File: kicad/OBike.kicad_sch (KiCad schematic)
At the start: 58 parts, among them J1 Conn_01x04, J3 Conn_01x02, J4 Conn_01x03, J5 Conn_01x08, J6 Conn_01x02, J7 Conn_01x04, J8 Micro_SD_Card_Det1, SW1 5_position_tactile, U1 DPS368XTSA1, U2 DS3231M, U3 MCP23017_SO, U4 74HC14, U5 Seeed Studio XIAO SAMD21

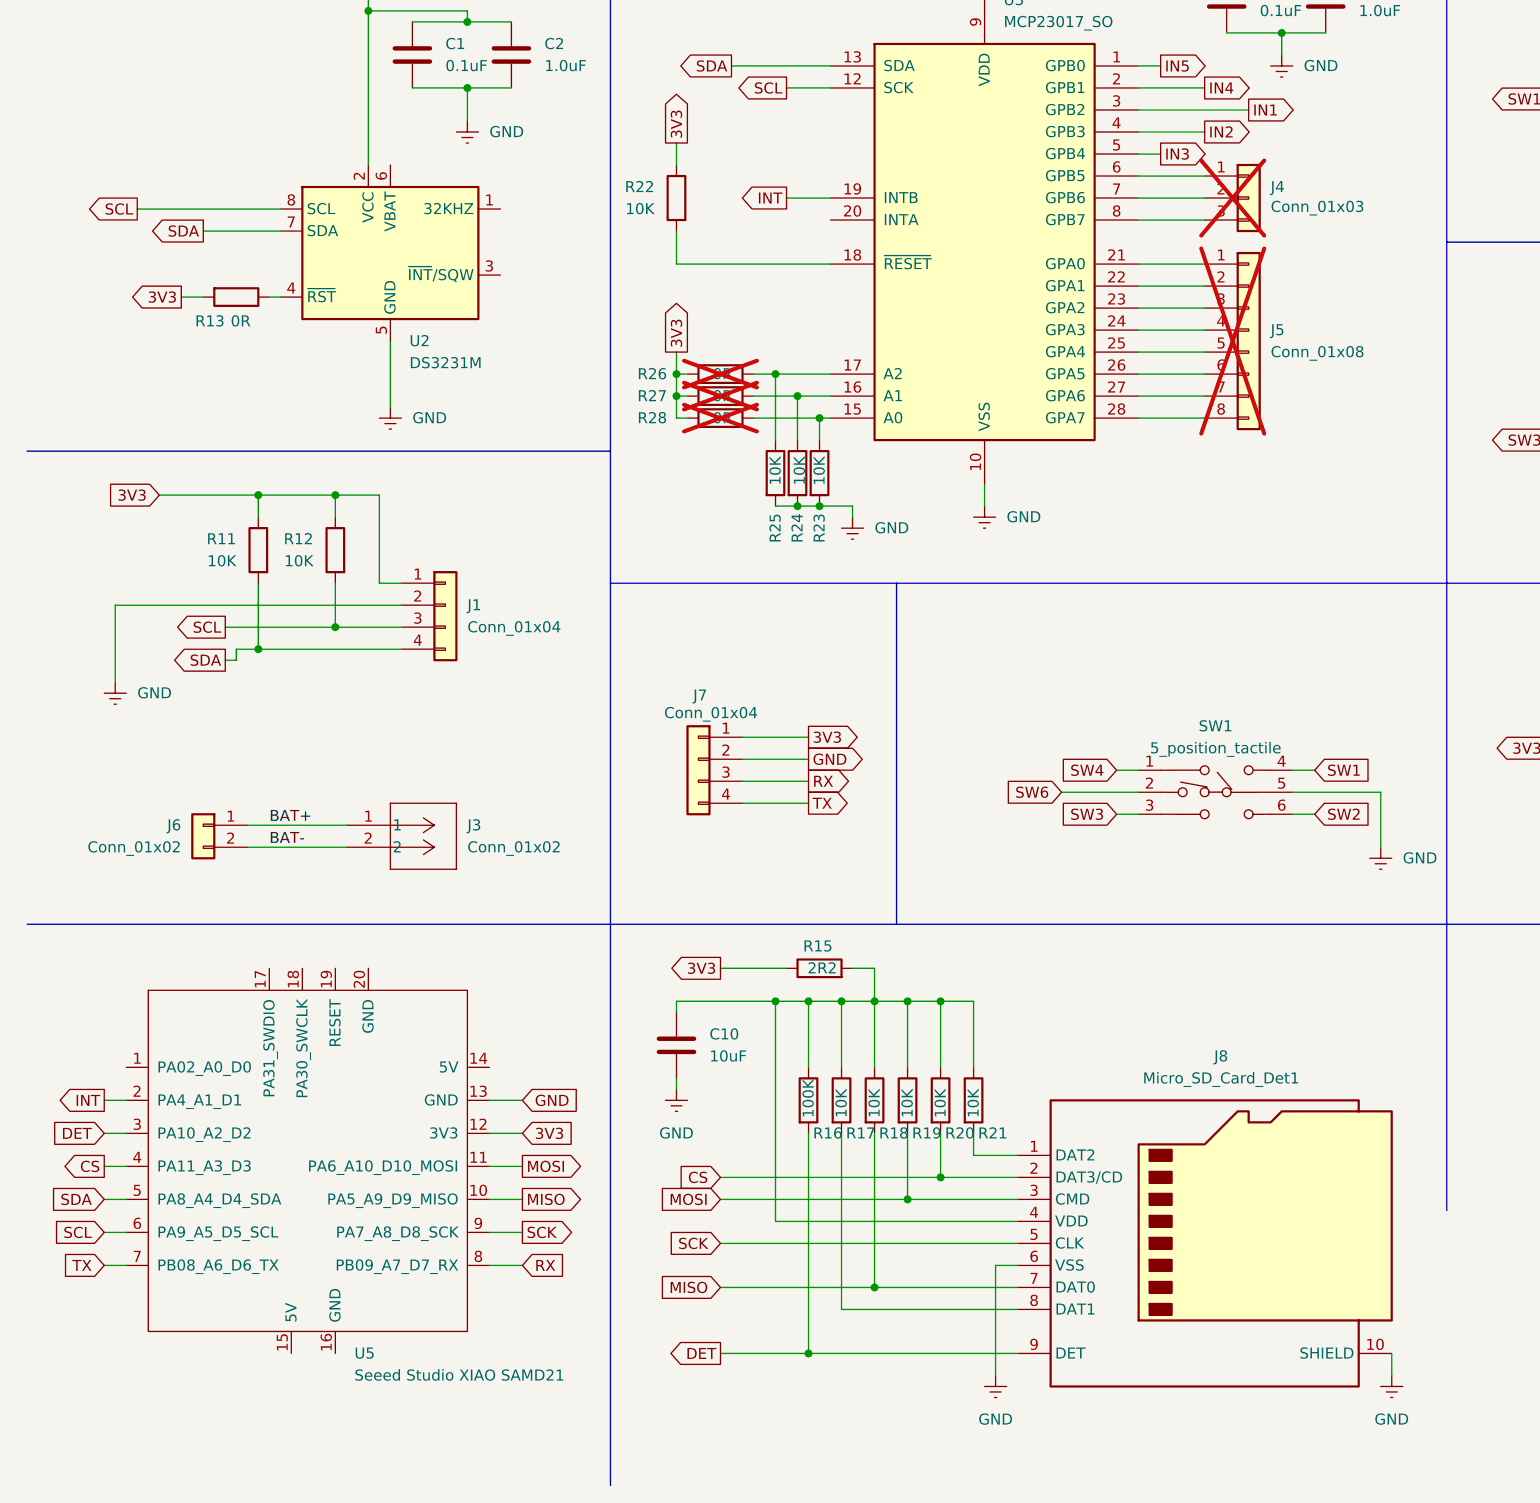
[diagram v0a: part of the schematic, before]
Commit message: 1.69" TFT
Changed screen connections to suit an SPI screen
Changed the arduino project to use the adafruit ST7789 library
Intended LCD is the wavshare 1.69" LCD
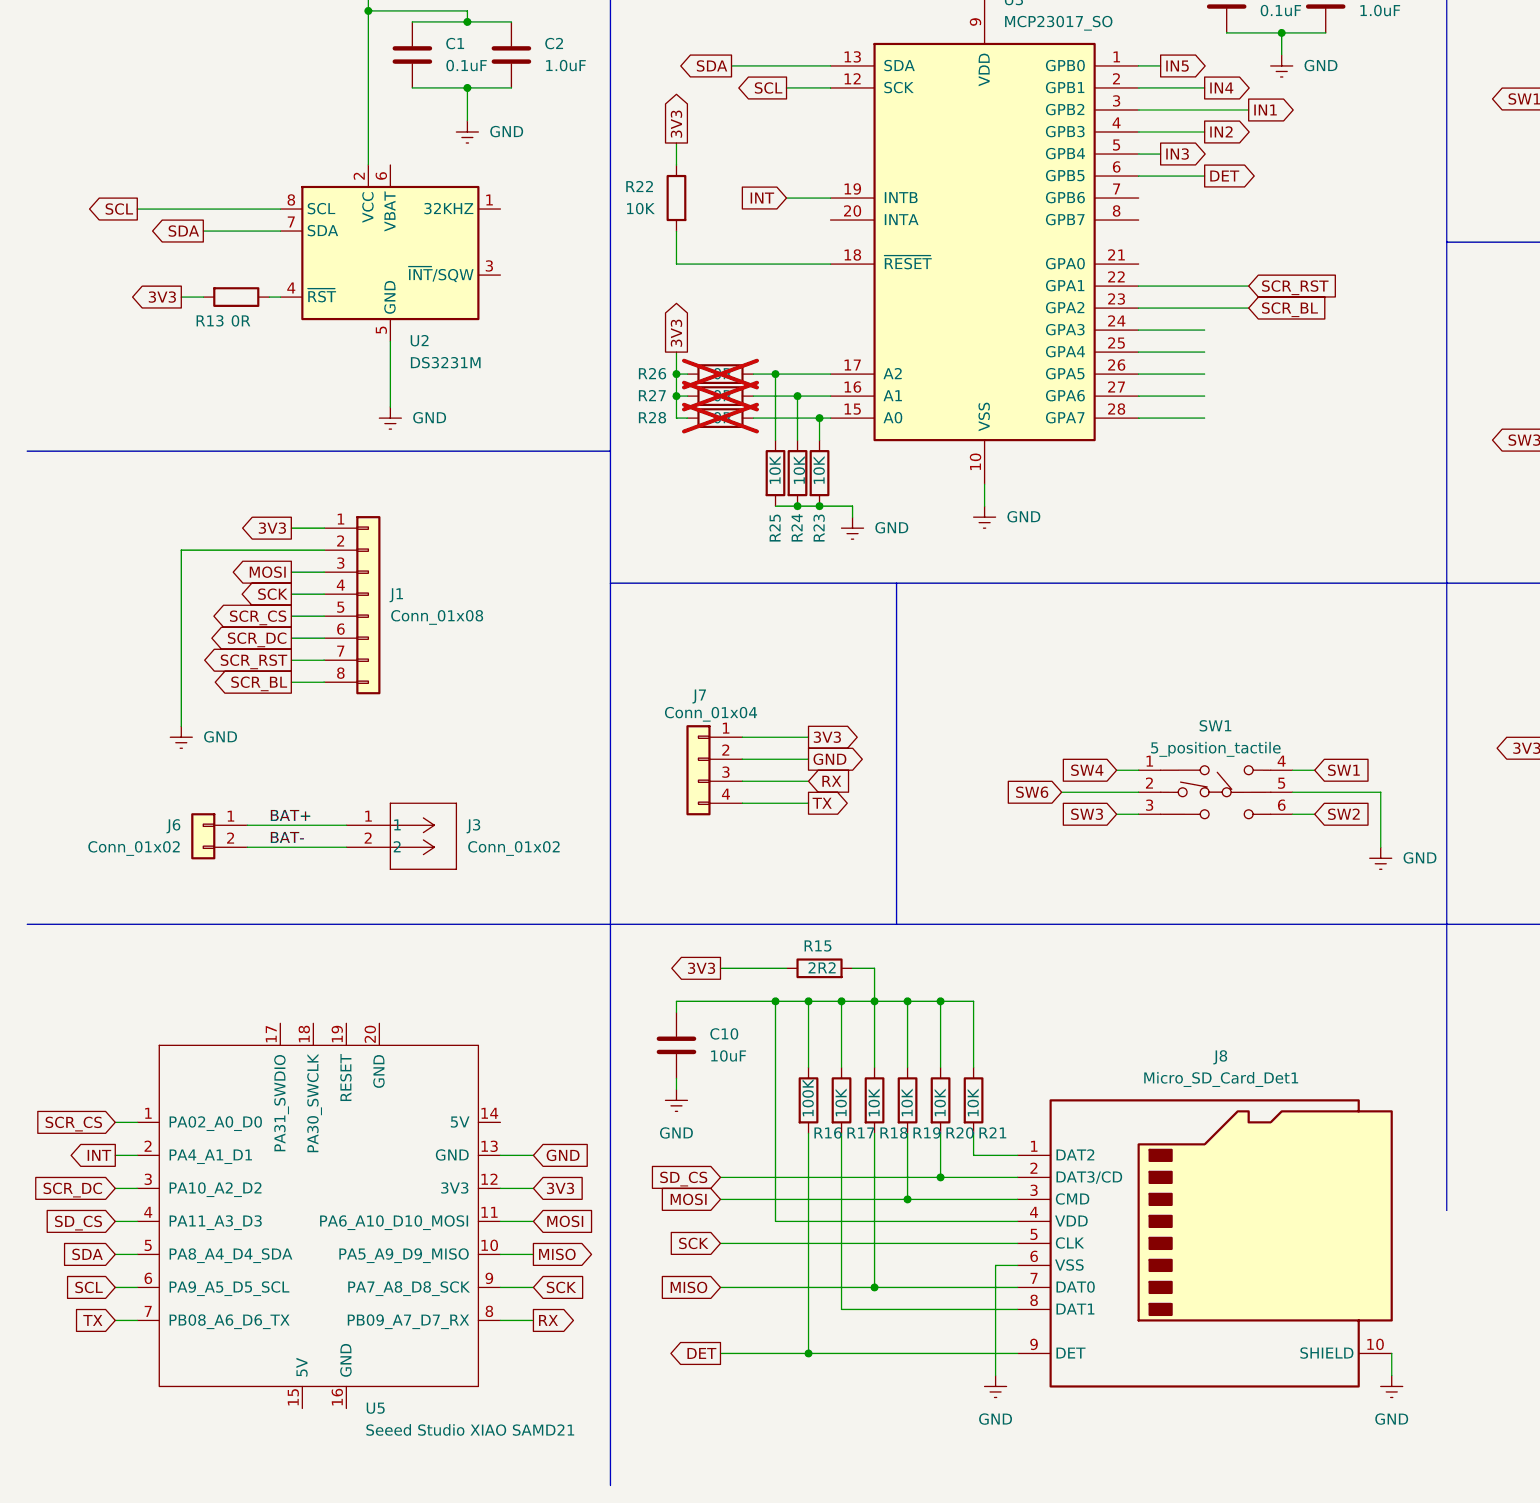
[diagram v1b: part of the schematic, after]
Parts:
- removed J1: Conn_01x04, Connector_PinHeader_2.54mm:PinHeader_1x04_P2.54mm_Vertical, symbol Connector_Generic:Conn_01x04
- removed J4: Conn_01x03, Connector_PinHeader_1.27mm:PinHeader_1x03_P1.27mm_Vertical, symbol Connector_Generic:Conn_01x03
- removed J5: Conn_01x08, Connector_PinHeader_1.27mm:PinHeader_1x08_P1.27mm_Vertical, symbol Connector_Generic:Conn_01x08
- removed R11, R12: 10K, Resistor_SMD:R_0805_2012Metric, symbol Device:R
- added J1: Conn_01x08, Connector_JST:JST_GH_SM08B-GHS-TB_1x08-1MP_P1.25mm_Horizontal, symbol Connector_Generic:Conn_01x08
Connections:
- net 3V3: now also J1.1 (Pin_1)
- net DET: now also U3.6 (GPB5); no longer U5.3 (PA10_A2_D2)
- net GND: now also J1.2 (Pin_2)
- net MOSI: now also J1.3 (Pin_3)
- net SCK: now also J1.4 (Pin_4)
- net SCR_RST: now reaches U3.22 (GPA1)
- net SCR_RST: now also J1.7 (Pin_7)
- net SCR_BL: now reaches U3.23 (GPA2)
- net SCR_BL: now also J1.8 (Pin_8)
- net SCR_CS: now reaches U5.1 (PA02_A0_D0)
- net SCR_CS: now also J1.5 (Pin_5)
- net CS renamed SD_CS
- new net SCR_DC: J1.6 (Pin_6), U5.3 (PA10_A2_D2)
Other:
- moved on the sheet: U5

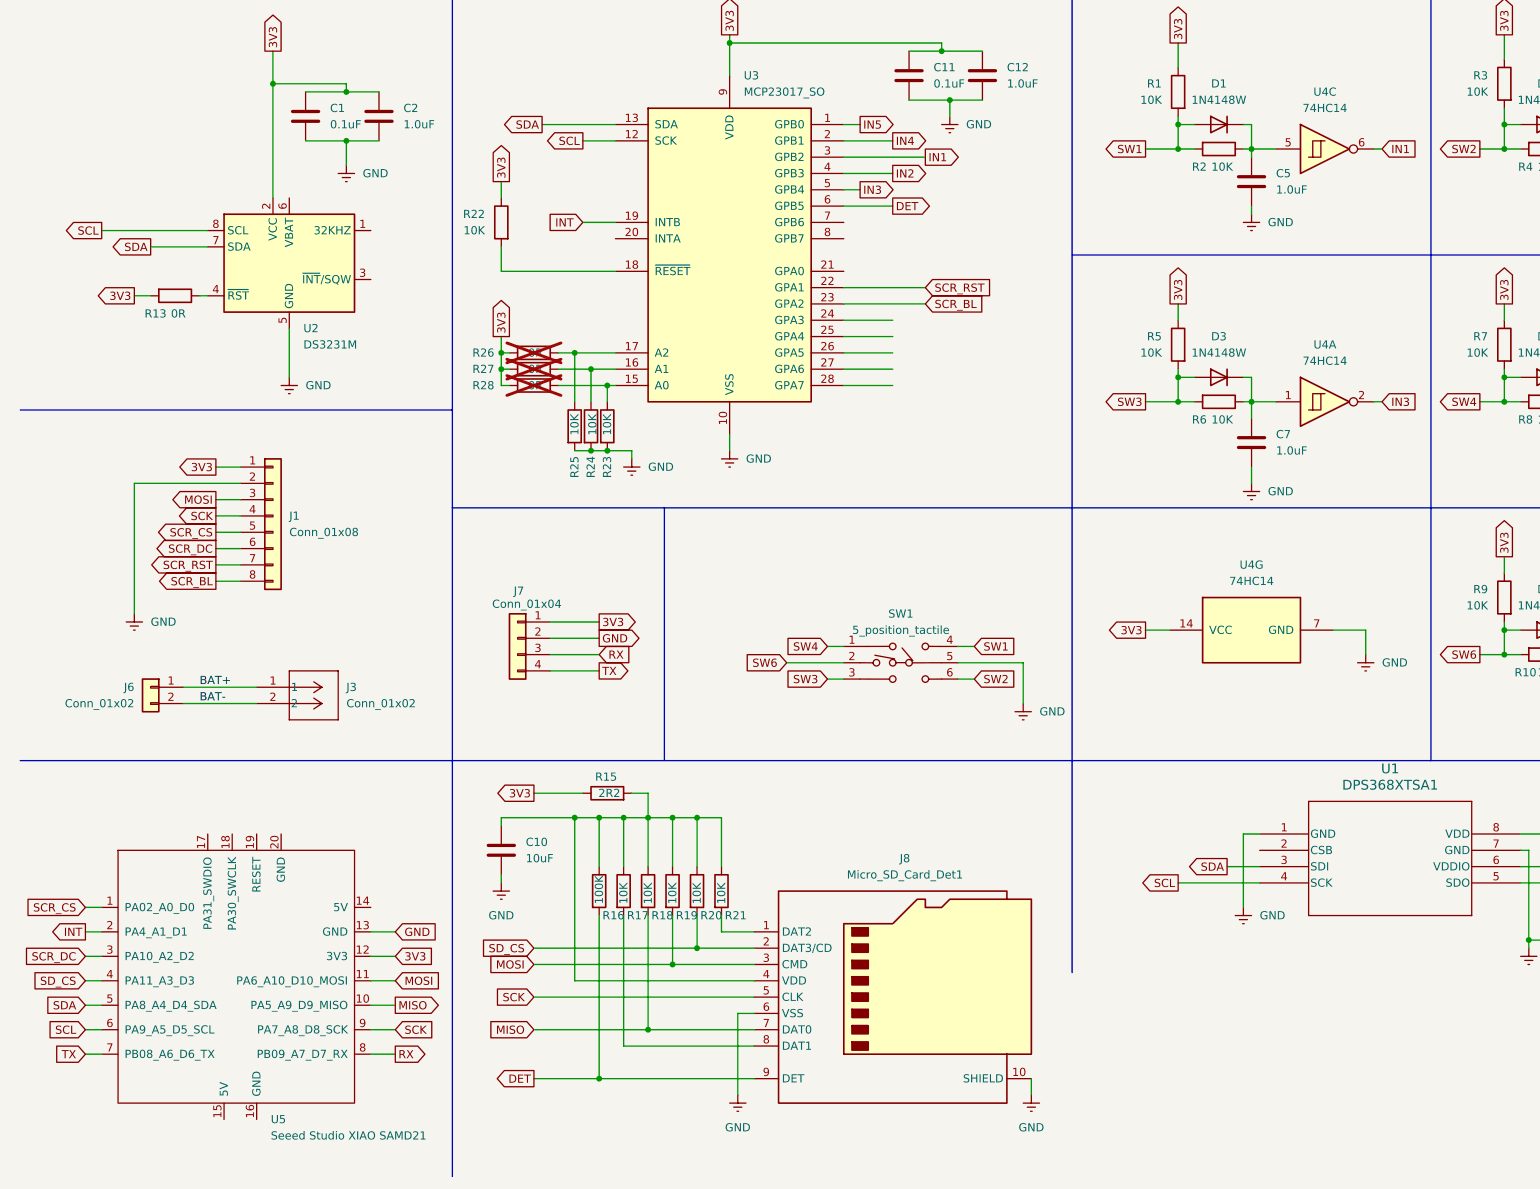
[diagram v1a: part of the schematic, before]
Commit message: gps added
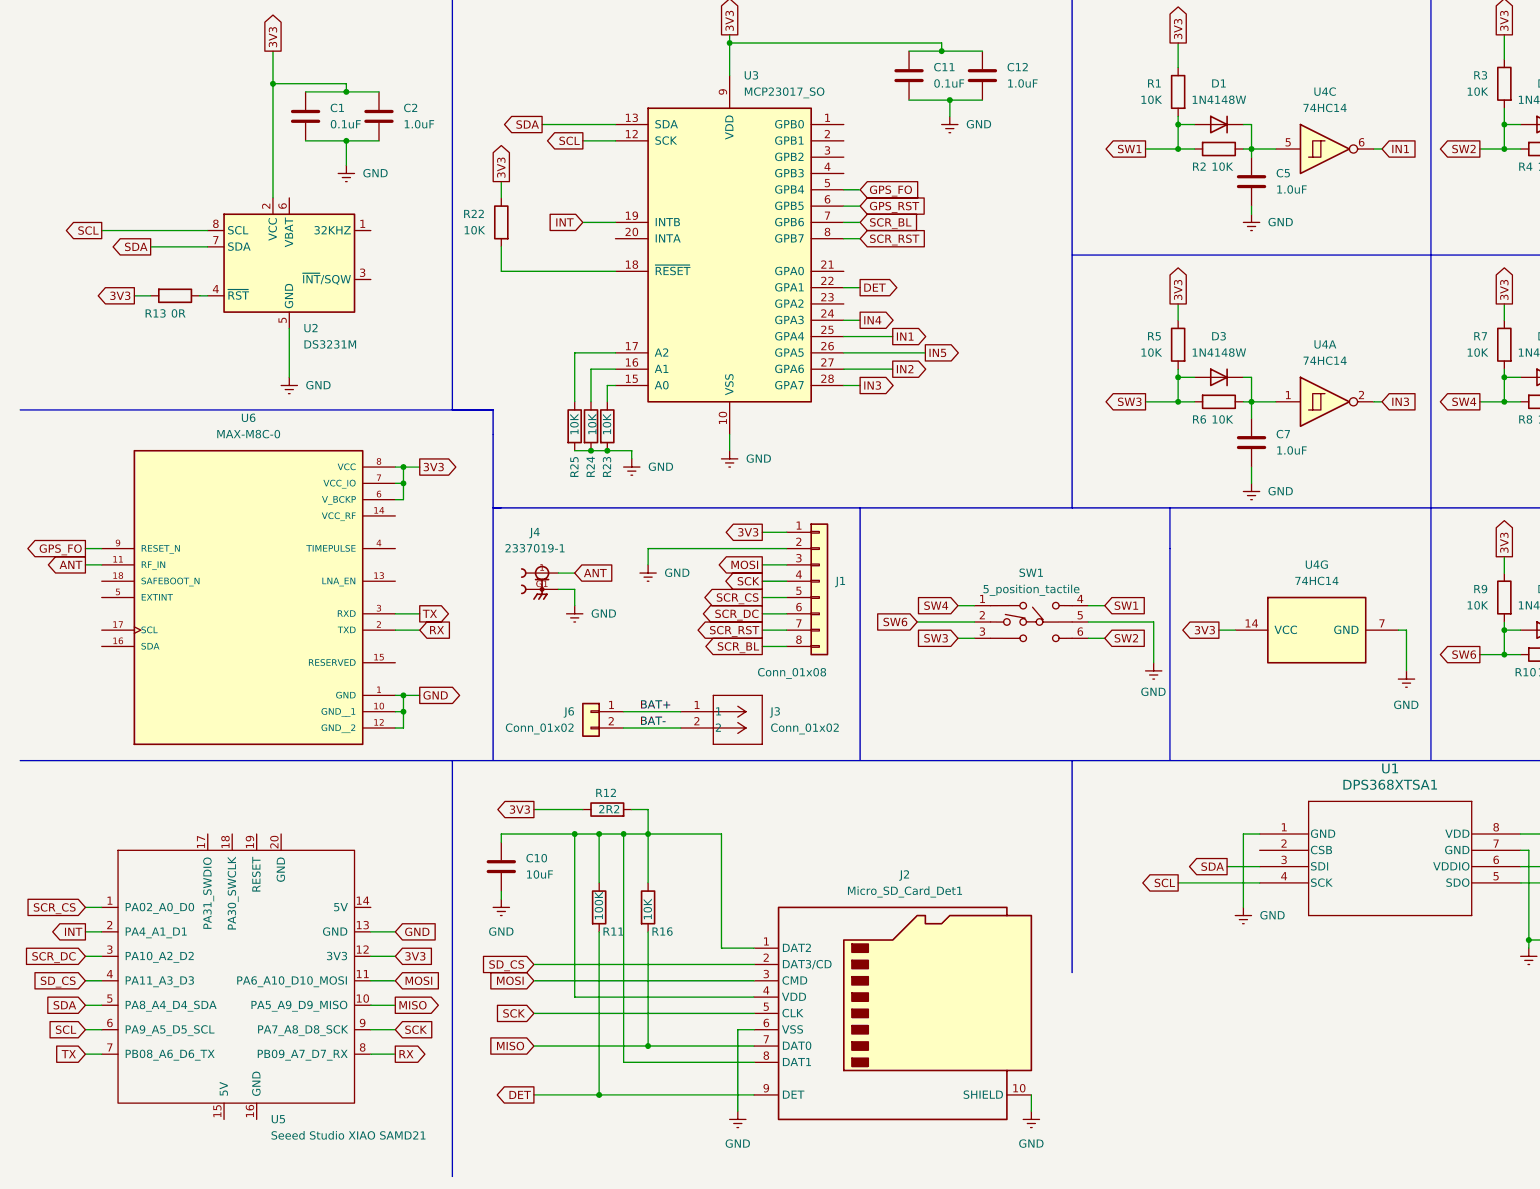
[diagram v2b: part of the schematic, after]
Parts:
- removed J7: Conn_01x04, Connector_PinHeader_1.27mm:PinHeader_1x04_P1.27mm_Vertical, symbol Connector_Generic:Conn_01x04
- removed J8: Micro_SD_Card_Det1, CUI-devices:MSD-11-A, symbol Connector:Micro_SD_Card_Det1
- removed R15: 2R2, Resistor_SMD:R_0805_2012Metric, symbol Device:R
- removed R17, R18, R19, R20, R21: 10K, Resistor_SMD:R_0805_2012Metric, symbol Device:R
- removed R26, R27, R28: 0R, Resistor_SMD:R_0603_1608Metric, symbol Device:R
- added J2: Micro_SD_Card_Det1, CUI-devices:CUI_MSD-11-A, symbol Connector:Micro_SD_Card_Det1
- added J4: 2337019-1, TE Connectivity:TE_2337019-1, symbol TE Connectivity:2337019-1
- added R11: 100K, Resistor_SMD:R_0603_1608Metric, symbol Device:R
- added R12: 2R2, Resistor_SMD:R_0603_1608Metric, symbol Device:R
- added U6: MAX-M8C-0, uBlox:XCVR_MAX-M8C-0, symbol uBlox:MAX-M8C-0
- C10: footprint Capacitor_SMD:C_0805_2012Metric -> Capacitor_SMD:C_0603_1608Metric
- R16: value 100K -> 10K; footprint Resistor_SMD:R_0805_2012Metric -> Resistor_SMD:R_0603_1608Metric
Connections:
- net 3V3: now also R12.1, U6.6 (V_BCKP), U6.7 (VCC_IO), U6.8 (VCC)
- net DET: now also U3.22 (GPA1), J2.9 (DET), R11.2; no longer R16.2, U3.6 (GPB5)
- net GND: now also J2.10 (SHIELD), J2.6 (VSS), J4.G1, U6.1 (GND), U6.10 (GND__1), U6.12 (GND__2)
- net IN1: now also U3.25 (GPA4); no longer U3.3 (GPB2)
- net IN2: now also U3.27 (GPA6); no longer U3.4 (GPB3)
- net IN3: now also U3.28 (GPA7); no longer U3.5 (GPB4)
- net IN4: now also U3.24 (GPA3); no longer U3.2 (GPB1)
- net IN5: now also U3.26 (GPA5); no longer U3.1 (GPB0)
- net MISO: now also R16.2, J2.7 (DAT0)
- net MOSI: now also J2.3 (CMD)
- net RX: now also U6.2 (TXD)
- net SCK: now also J2.5 (CLK)
- net SCR_BL: now also U3.7 (GPB6); no longer U3.23 (GPA2)
- net SCR_RST: now also U3.8 (GPB7); no longer U3.22 (GPA1)
- net SD_CS: now also J2.2 (DAT3/CD)
- net TX: now also U6.3 (RXD)
- net at C10.1, R16.1: now also J2.1 (DAT2), J2.4 (VDD), J2.8 (DAT1), R11.1, R12.2
- new net ANT: J4.1, U6.11 (RF_IN)
- new net GPS_FO: U3.5 (GPB4), U6.9 (RESET_N)
- new net GPS_RST: U3.6 (GPB5)
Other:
- moved on the sheet: J1, J3, J6, SW1, U4G
